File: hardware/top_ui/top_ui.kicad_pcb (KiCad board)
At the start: 2 copper layers, 47 x 47 mm, 27 parts, among them J1 USB-C, J2 J_STK_A, J3 J_STK_B, J5 ST7789 240x280, J6 Stern Klinke, J7 Reserve UART, Q1 BC847, Q2 P-FET 20V 1A, SW1 BTN1, SW2 BTN2, SW3 BTN3, SW4 BTN4, U1 USBLC6-2SC6, U2 SHT40-AD1B, U3 VL53L1X

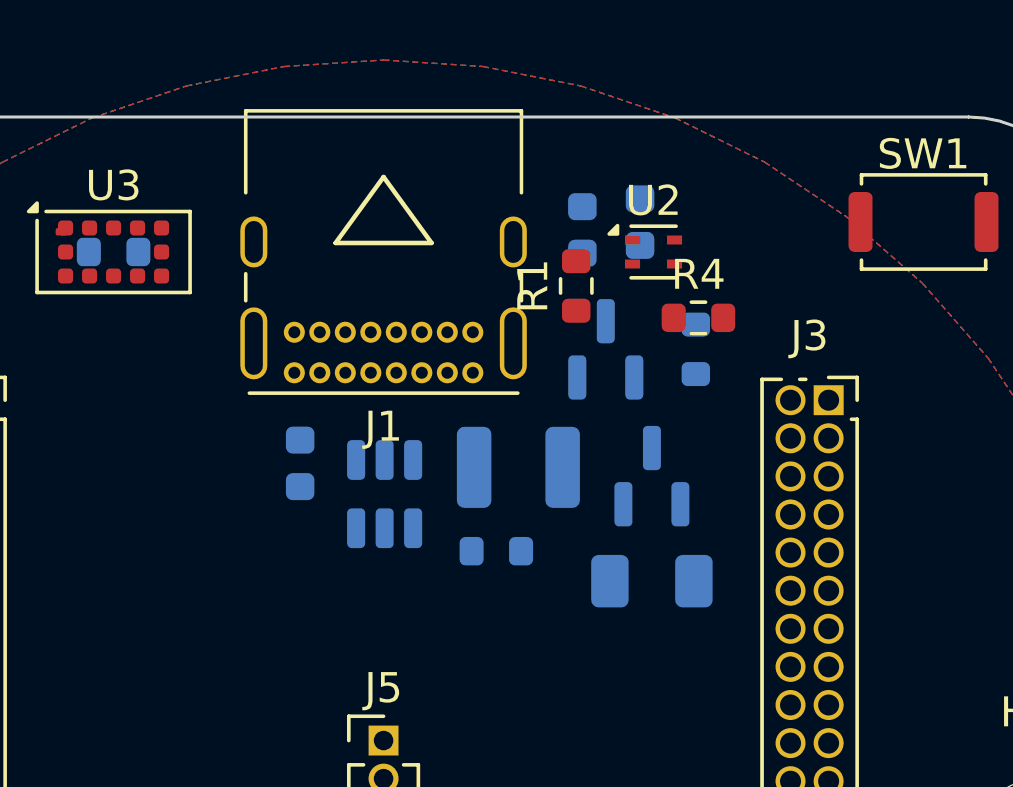
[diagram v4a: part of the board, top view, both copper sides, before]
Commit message: Stehende USB-C-Buchse, Nutzen mit gemischter Geometrie - Top ist DRC-sauber
USB-C (Punkt 45)
----------------
Gewaehlt: G-Switch GT-USB-7051x, vertikal SMT, 22 Pads (A- und B-Reihe
vollstaendig, also steckrichtungsunabhaengig), Footprint 9,94 x 6,40 mm,
LCSC C2843970. Sie sitzt mittig oben, zeigt nach vorn und liegt unter der
Zentralscheibe - erreichbar erst nach deren Abnahme, so wie es Punkt 45
verlangt.

Der Nebeneffekt ist der eigentliche Gewinn: Die 28 clearance-Meldungen, die das
Top-Board seit dem ersten Layout begleitet haben, sind verschwunden. Sie waren
nie ein Layoutfehler, sondern die zu eng gerasterten Pads der liegenden GCT
USB4085 gegen unsere 0,15-mm-Vorgabe. Das Top-Board meldet jetzt KEINEN
DRC-Fehler mehr - nur noch drei bewusste Randverletzungen (zwei davon sind die
NPTH-Loecher der Buchse gegen ihre eigenen Pads, eine der Klinken-Platzhalter).

Der Waiver-Mechanismus in gen_layouts.py war dafuer zu grob: Er hat nur auf das
Zeilenende geprueft. Jetzt wird nur gewaivert, wenn ALLE in der Meldung
genannten Bauteile in der Ausnahmeliste stehen - sonst verschluckt ein Waiver
fuer J1 auch eine echte Kollision J1 gegen U3.

Fertigungsnutzen
----------------
gen_panel.py beherrscht gemischte Geometrie: zwei Kreise Oe52 und ein
abgerundetes Quadrat 47 x 47. Das Quadrat bekommt seine Fraesfuge als
Parallelkurve der Kontur, mit vier Stegen - je einer pro Kante, um 10 mm aus der
Mitte versetzt, weil dort entweder eine Befestigungsbohrung oder der
ueberstehende Klinken-Platzhalter sitzt. 173,4 x 64,4 mm = 112 cm2.

Zwei Fehler dabei gefunden und behoben: Die geschlossene Konturliste endete auf
ihrem eigenen Anfangspunkt - beim Umlauf entstand ein Segment der Laenge null,
und KiCad meldete die ganze Kontur als ungueltig. Und die Seitennamen der Stege
sind KiCad-Koordinaten mit y nach unten; die erste Fassung setzte den Steg
deshalb genau auf die Klinke.

Der DRC des Nutzens ist wieder deckungsgleich mit der Summe der Einzelboards.

Co-Authored-By: Claude Opus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
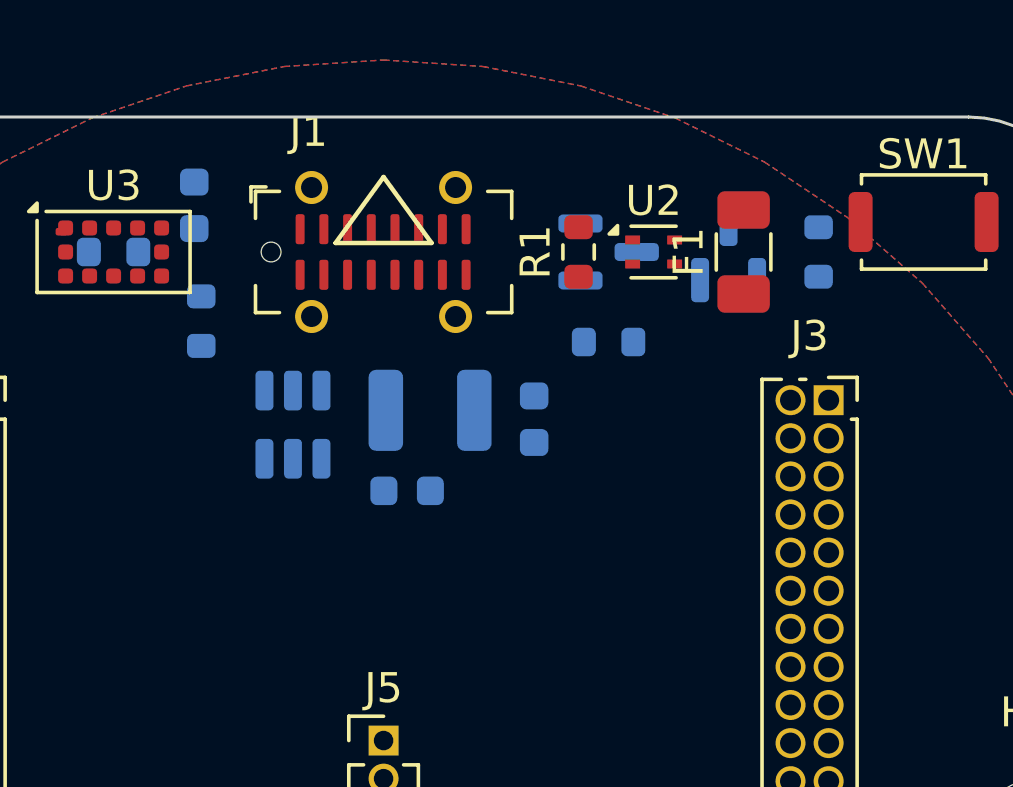
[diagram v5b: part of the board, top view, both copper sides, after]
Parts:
- F1: moved to F.Cu
- J1: footprint USB_C_Receptacle_GCT_USB4085 -> USB_C_Receptacle_G-Switch_GT-USB-7051x
- R4: moved to B.Cu
- moved C1 13.0 mm to (-6.31, -20.6)
- moved R2 12.5 mm to (-6.08, -16.7), turned to 90 degrees
- moved C4 11.9 mm to (0.78, -11.0), turned to 0 degrees
- moved F1 11.4 mm to (12.0, -19.0), turned to 90 degrees
- moved C3 7.94 mm to (5.02, -13.4)
- moved Q2 7.90 mm to (11.5, -19.0)
- moved J1 5.01 mm to (0.00, -19.0), turned to 0 degrees
- moved R4 4.57 mm to (14.5, -19.0), turned to 90 degrees
- moved U1 3.83 mm to (-3.02, -13.2)
- moved C2 3.50 mm to (1.55, -13.7)
- moved Q1 3.24 mm to (7.50, -19.0), turned to 0 degrees
- moved R3 2.92 mm to (7.50, -16.0), turned to 0 degrees
- moved R1 1.14 mm to (6.50, -19.0)

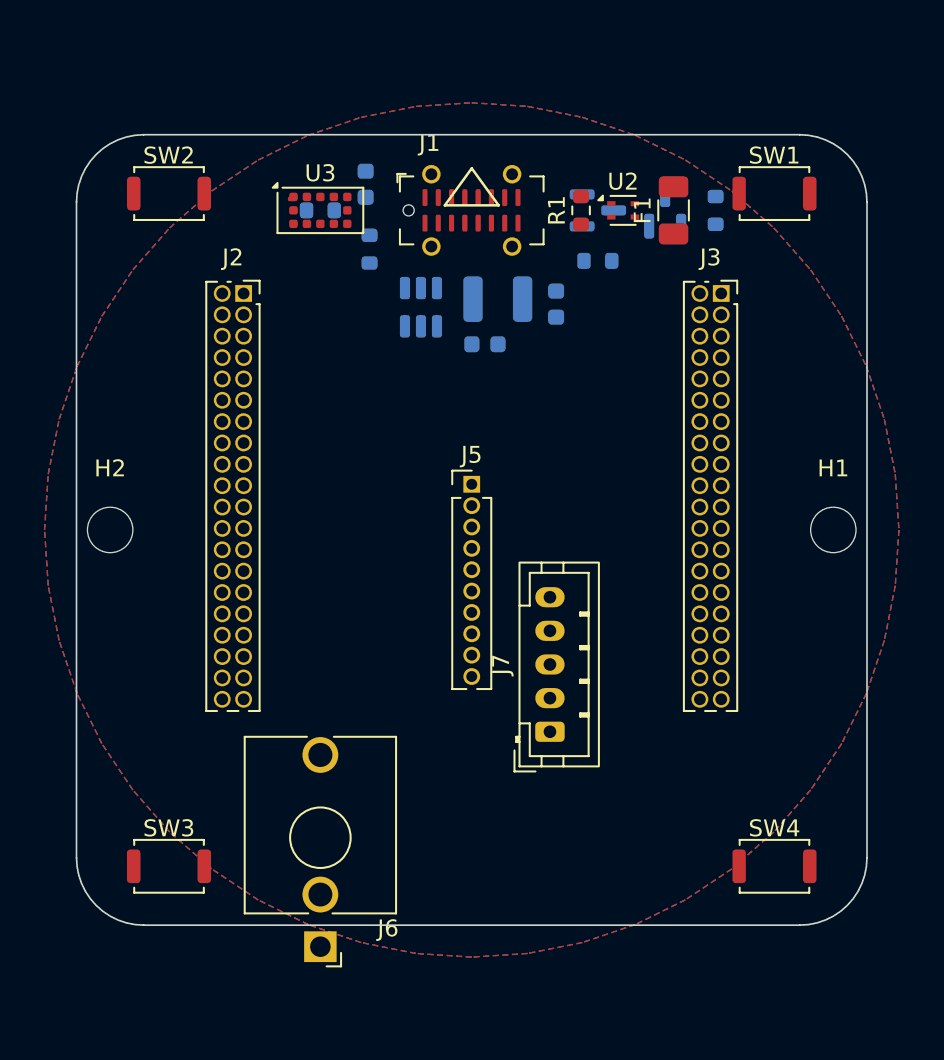
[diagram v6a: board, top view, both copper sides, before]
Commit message: Top geroutet: 197 Segmente, 12 Vias - Tasten und USB blieben offen
Der Lauf war schnell, das Ergebnis duenn:

  197 Bahnsegmente, 12 Vias
  offen: 57 auf PGND/AGND (schliesst die Zonenfuellung)
         14 Signale

Unter den offenen Signalen sind ausgerechnet die, auf die es ankommt: BTN1 bis
BTN4 vollstaendig - also alle vier Ecktaster - sowie USB_VBUS dreimal,
USB_DP_C zweimal und USB_CC2. Die USB-Ecke und die Tastenanbindung an den
Stackverbinder sind die beiden Stellen, an denen der Router aufgegeben hat.

Dazu eine neue Kollision, die vorher nicht da war: Der Router hat STAR_OUT auf
B.Cu durch das Befestigungsloch der USB-Buchse gelegt. Zwei DRC-Meldungen
(hole_clearance und copper_edge_clearance) aus derselben Ursache, an einer
Stelle zu beheben.

Die drei uebrigen Randmeldungen sind die bekannten: zweimal die NPTH-Loecher
der USB-Buchse gegen ihre eigenen Pads, einmal der Klinken-Platzhalter.

Vor dem Lauf war Top DRC-frei. Das ist kein Rueckschritt - ein Board ohne
Leiterbahnen kann keine Kupferfehler haben.

Co-Authored-By: Claude Opus 5 (1M context) <noreply@anthropic.com>
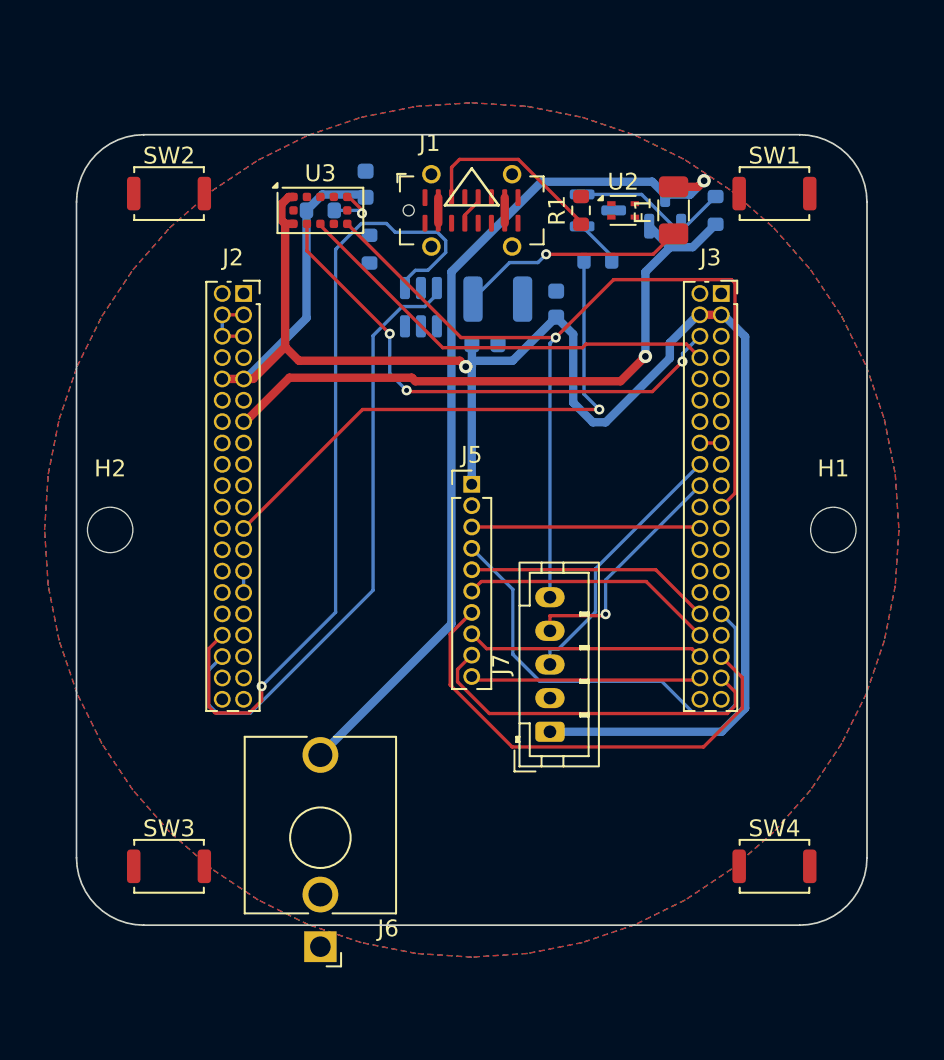
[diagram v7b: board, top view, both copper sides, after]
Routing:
- net 3V3_SYS: track 0.00 -> 110.5 mm, vias 0 -> 1
- net PRESENCE_INT: track 0.00 -> 56.6 mm, vias 0 -> 1
- net STAR_OUT: track 0.00 -> 51.8 mm, vias 0 -> 1
- net USB_DP: track 0.00 -> 48.7 mm, vias 0 -> 1
- net 6V2_STAR_F: track 0.00 -> 37.8 mm, vias 0 -> 1
- net USB_DN: track 0.00 -> 36.5 mm
- net STAR_EN: track 0.00 -> 33.3 mm, vias 0 -> 1
- net I2C_SCL: track 0.00 -> 31.5 mm, vias 0 -> 3
- net QSPI_D3: track 0.00 -> 28.3 mm
- net QSPI_D0: track 0.00 -> 28.0 mm
- net I2C_SDA: track 0.00 -> 26.1 mm
- net DISP_RST: track 0.00 -> 21.4 mm
- net UART_AUX_TX: track 0.00 -> 15.9 mm
- net QSPI_D2: track 0.00 -> 15.1 mm
- net QSPI_D1: track 0.00 -> 14.7 mm
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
